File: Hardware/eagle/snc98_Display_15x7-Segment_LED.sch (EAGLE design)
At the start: 67 parts

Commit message: PCB_Display_make
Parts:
- removed C10, C11, C12: 15n, rcl:C-EUC1206K
- removed D1, D10, D11, D12, D13, D29, D3, D4, D5: SD103CW, BaseApp:DIODESMA-WIDE
- removed D6, D7, D8, D9: SD103C, BaseApp:DIODE280MIL-TH
- removed H1, H10, H2, H3, H4, H5, H6, H7, H8, H9: MOUNT-PAD-ROUND2.8, holes:MOUNT-PAD-ROUND2.8
- removed JP1: (no value), SparkFun-Connectors:M09LOCK-LONGPADS
- removed R1, R2, R3: 6k8, rcl:R-EU_R1206
- removed R23, R25, R27: 27k, rcl:R-EU_0204/5
- removed R24, R26, R28: 6k8, rcl:R-EU_0204/5
- removed R4: 27k, rcl:R-EU_R1206
- removed S1, S10, S11, S12, S2, S3, S4, S5, S6, S7, S8, S9: B3F-4150, SmartPrj:TACTILE_SWITCHTACTILE_SWITCH_PTH-12MM
- added BH4, BH5: HOLDER_AAA_LEFT1, SparkFun-Electromechanical:HOLDER_AAA_LEFT1
- added BH6: HOLDER_AAA_RIGHT, SparkFun-Electromechanical:HOLDER_AAA_RIGHT
- added JP10, JP11, JP12, JP7, JP8, JP9: (no value), adafruit:PINHD-1X1
- added LOGO3: OSHW_LOGO_6MILX0100-NT, ohw-logo:OSHW_LOGO_6MILX0100-NT
- added M10, M11, M4, M5, M6, M7, M8, M9: IRLML6402, IRLML6402:IRLML6402
- added R10, R11, R12, R13, R14, R15, R16, R17, R18, R19, R7, R8, R9: 22, rcl:R-EU_R1210
- added R29, R30, R54, R55, R56, R57, R58, R59: 3k3, rcl:R-EU_0204/5
- added R36, R37, R38, R39, R40, R41, R42, R43: 3k3, rcl:R-EU_R1206
- added X1, X3: MICROMATCH-12, Con-amp-micromatch:MICROMATCH-12
- D14, D15, D2: value SD103CW -> SC40-11_UNISC40-11_UNI; device BaseApp:DIODESMA-WIDE -> display-hp:SC40-11_UNISC40-11_UNI
- D16, D17, D18, D19, D20, D21: value BAT54A -> SC40-11_UNISC40-11_UNI; device diode:BAT54A -> display-hp:SC40-11_UNISC40-11_UNI
- D22, D23, D24, D25, D26, D27: value SD103C -> SC40-11_UNISC40-11_UNI; device BaseApp:DIODE280MIL-TH -> display-hp:SC40-11_UNISC40-11_UNI
- R5, R6: value 27k -> 22; device rcl:R-EU_R1206 -> rcl:R-EU_R1210
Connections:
- removed net A1: C10.1, JP1.6, R1.2, R23.1, R24.2, R4.1
- removed net A2: C11.1, JP1.7, R2.2, R25.1, R26.2, R5.1
- removed net A3: C12.1, JP1.8, R27.1, R28.2, R3.2, R6.1
- removed net AREF: JP1.9, R23.2, R25.2, R27.2, R4.2, R5.2, R6.2
- removed net A_1: D1.A, D12.A, D13.A, D16.AA, D17.AA, D23.A, D24.A, D27.A, D29.A, R1.1, R24.1
- removed net A_2: D11.A, D14.A, D18.AA, D19.AA, D2.A, D22.A, D25.A, D26.A, D5.A, R2.1, R26.1
- removed net A_3: D10.A, D15.A, D20.AA, D21.AA, D3.A, D4.A, D6.A, D7.A, D8.A, D9.A, R28.1, R3.1
- removed net C1: JP1.2, S1.1, S1.2, S5.1, S5.2, S9.1, S9.2
- removed net C2: JP1.3, S10.1, S10.2, S2.1, S2.2, S6.1, S6.2
- removed net C3: JP1.4, S11.1, S11.2, S3.1, S3.2, S7.1, S7.2
- removed net C4: JP1.5, S12.1, S12.2, S4.1, S4.2, S8.1, S8.2
- removed net GND: C10.2, C11.2, C12.2, JP1.1, S1.5, S10.5, S11.5, S12.5, S2.5, S3.5, S4.5, S5.5, S6.5, S7.5, S8.5, S9.5
- removed net N$16: D15.C, D20.K1, D6.C, S9.3, S9.4
- removed net N$18: D10.C, D20.K2, D7.C, S10.3, S10.4
- removed net N$19: D12.C, D16.K2, D27.C, S2.3, S2.4
- removed net N$2: D1.C, D17.K2, D23.C, S4.3, S4.4
- removed net N$21: D21.K1, D4.C, D8.C, S11.3, S11.4
- removed net N$22: D21.K2, D3.C, D9.C, S12.3, S12.4
- removed net N$24: D14.C, D18.K1, S5.3, S5.4
- removed net N$25: D11.C, D18.K2, D26.C, S6.3, S6.4
- removed net N$28: D19.K1, D25.C, D5.C, S7.3, S7.4
- removed net N$30: D19.K2, D2.C, D22.C, S8.3, S8.4
- removed net N$32: D17.K1, D24.C, D29.C, S3.3, S3.4
- removed net N$6: D13.C, D16.K1, S1.3, S1.4
- new net CA_LED: M10.S, M11.S, M4.S, M5.S, M6.S, M7.S, M8.S, M9.S, R29.1, R30.1, R36.1, R37.1, R38.1, R39.1, R40.1, R41.1, R42.1, R43.1, R54.1, R55.1, R56.1, R57.1, R58.1, R59.1, X3-8.S
- new net D0_A: R5.2, X3-1.S
- new net D10_A: R15.2, X1-8.S
- new net D11_A: R16.2, X1-9.S
- new net D12_A: R17.2, X1-10.S
- new net D13_A: R18.2, X1-11.S
- new net D14_A: R19.2, X1-12.S
- new net D1_A: R6.2, X3-2.S
- new net D2_A: R7.2, X3-3.S
- new net D3_A: R8.2, X3-4.S
- new net D4_A: R9.2, X3-5.S
- new net D5_A: R10.2, X3-6.S
- new net D6_A: R11.2, X3-7.S
- new net D7_A: R12.2, X1-5.S
- new net D8_A: R13.2, X1-6.S
- new net D9_A: R14.2, X1-7.S
- new net DIG_0: D2.CC1, D2.CC2, D2.CC3, D2.CC4, R5.1
- new net DIG_1: D14.CC1, D14.CC2, D14.CC3, D14.CC4, R6.1
- new net DIG_10: D23.CC1, D23.CC2, D23.CC3, D23.CC4, R15.1
- new net DIG_11: D24.CC1, D24.CC2, D24.CC3, D24.CC4, R16.1
- new net DIG_12: D25.CC1, D25.CC2, D25.CC3, D25.CC4, R17.1
- new net DIG_13: D26.CC1, D26.CC2, D26.CC3, D26.CC4, R18.1
- new net DIG_14: D27.CC1, D27.CC2, D27.CC3, D27.CC4, R19.1
- new net DIG_2: D15.CC1, D15.CC2, D15.CC3, D15.CC4, R7.1
- new net DIG_3: D16.CC1, D16.CC2, D16.CC3, D16.CC4, R8.1
- new net DIG_4: D17.CC1, D17.CC2, D17.CC3, D17.CC4, R9.1
- new net DIG_5: D18.CC1, D18.CC2, D18.CC3, D18.CC4, R10.1
- new net DIG_6: D19.CC1, D19.CC2, D19.CC3, D19.CC4, R11.1
- new net DIG_7: D20.CC1, D20.CC2, D20.CC3, D20.CC4, R12.1
- new net DIG_8: D21.CC1, D21.CC2, D21.CC3, D21.CC4, R13.1
- new net DIG_9: D22.CC1, D22.CC2, D22.CC3, D22.CC4, R14.1
- new net IO-A: M4.G, R29.2, R36.2, X1-4.S
- new net IO-B: M5.G, R30.2, R37.2, X1-3.S
- new net IO-C: M6.G, R42.2, R54.2, X1-2.S
- new net IO-D: M7.G, R38.2, R55.2, X1-1.S
- new net IO-DP: M11.G, R41.2, R59.2, X3-9.S
- new net IO-E: M8.G, R43.2, R56.2, X3-12.S
- new net IO-F: M9.G, R39.2, R57.2, X3-11.S
- new net IO-G: M10.G, R40.2, R58.2, X3-10.S
- new net NC1: BH4.+
- new net NC2: BH5.+
- new net NC3: BH6.-
- new net SEG_A: D14.A, D15.A, D16.A, D17.A, D18.A, D19.A, D2.A, D20.A, D21.A, D22.A, D23.A, D24.A, D25.A, D26.A, D27.A, M4.D
- new net SEG_B: D14.B, D15.B, D16.B, D17.B, D18.B, D19.B, D2.B, D20.B, D21.B, D22.B, D23.B, D24.B, D25.B, D26.B, D27.B, M5.D
- new net SEG_C: D14.C, D15.C, D16.C, D17.C, D18.C, D19.C, D2.C, D20.C, D21.C, D22.C, D23.C, D24.C, D25.C, D26.C, D27.C, JP11.1, JP8.1
- new net SEG_C_SOURCE: JP10.1, M6.D
- new net SEG_D: D14.D, D15.D, D16.D, D17.D, D18.D, D19.D, D2.D, D20.D, D21.D, D22.D, D23.D, D24.D, D25.D, D26.D, D27.D, M7.D
- new net SEG_DP: D14.DP, D14.DP1, D15.DP, D15.DP1, D16.DP, D16.DP1, D17.DP, D17.DP1, D18.DP, D18.DP1, D19.DP, D19.DP1, D2.DP, D2.DP1, D20.DP, D20.DP1, D21.DP, D21.DP1, D22.DP, D22.DP1, D23.DP, D23.DP1, D24.DP, D24.DP1, D25.DP, D25.DP1, D26.DP, D26.DP1, D27.DP, D27.DP1, JP12.1, JP9.1
- new net SEG_DP_SOURCE: JP7.1, M11.D
- new net SEG_E: D14.E, D15.E, D16.E, D17.E, D18.E, D19.E, D2.E, D20.E, D21.E, D22.E, D23.E, D24.E, D25.E, D26.E, D27.E, M8.D
- new net SEG_F: D14.F, D15.F, D16.F, D17.F, D18.F, D19.F, D2.F, D20.F, D21.F, D22.F, D23.F, D24.F, D25.F, D26.F, D27.F, M9.D
- new net SEG_G: D14.G, D14.G1, D15.G, D15.G1, D16.G, D16.G1, D17.G, D17.G1, D18.G, D18.G1, D19.G, D19.G1, D2.G, D2.G1, D20.G, D20.G1, D21.G, D21.G1, D22.G, D22.G1, D23.G, D23.G1, D24.G, D24.G1, D25.G, D25.G1, D26.G, D26.G1, D27.G, D27.G1, M10.D
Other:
- note added: "0.8"
- note added: "Calculator 15-Digit with 1284P"
- note added: "Calculator 15-Digit with ATmega1284P by Jens Grabner is licensed under"
- note removed: "0.3"
- note removed: "snc98 3x4 Switch-block"
- note removed: "snc98 3x4 Switch-block Rev. 0.3 by Jens Grabner is licensed under"

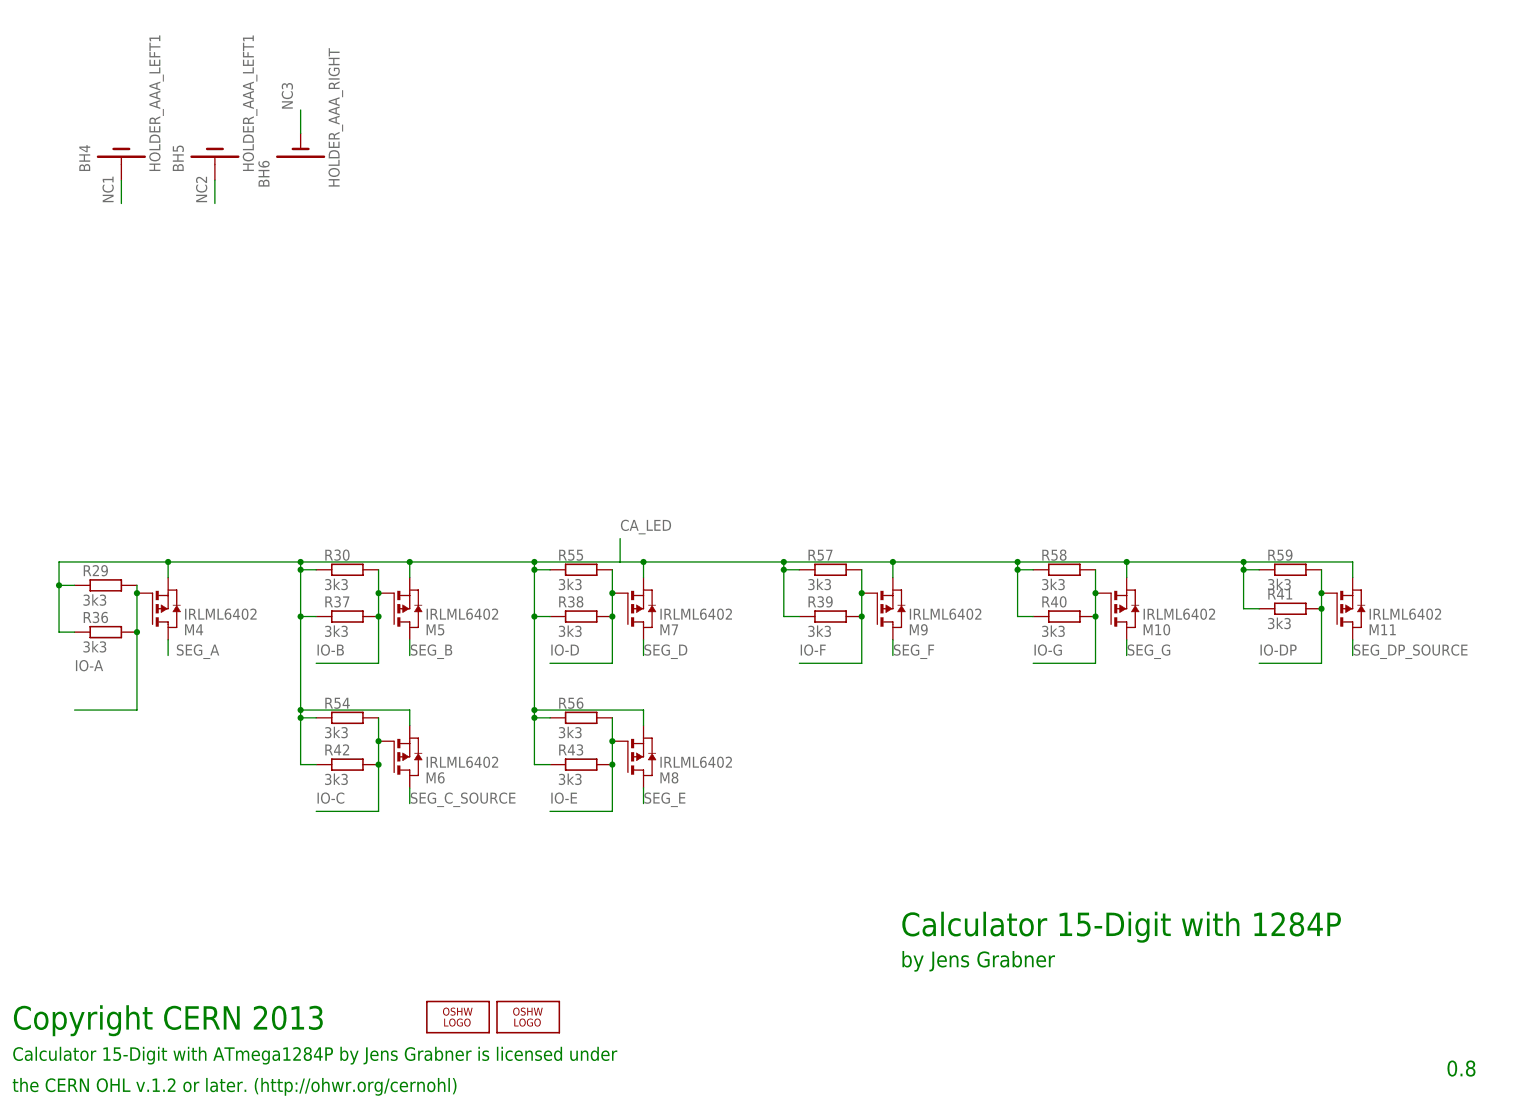
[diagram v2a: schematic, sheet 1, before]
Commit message: snc98_Display_15x7-Segment_LED_v2
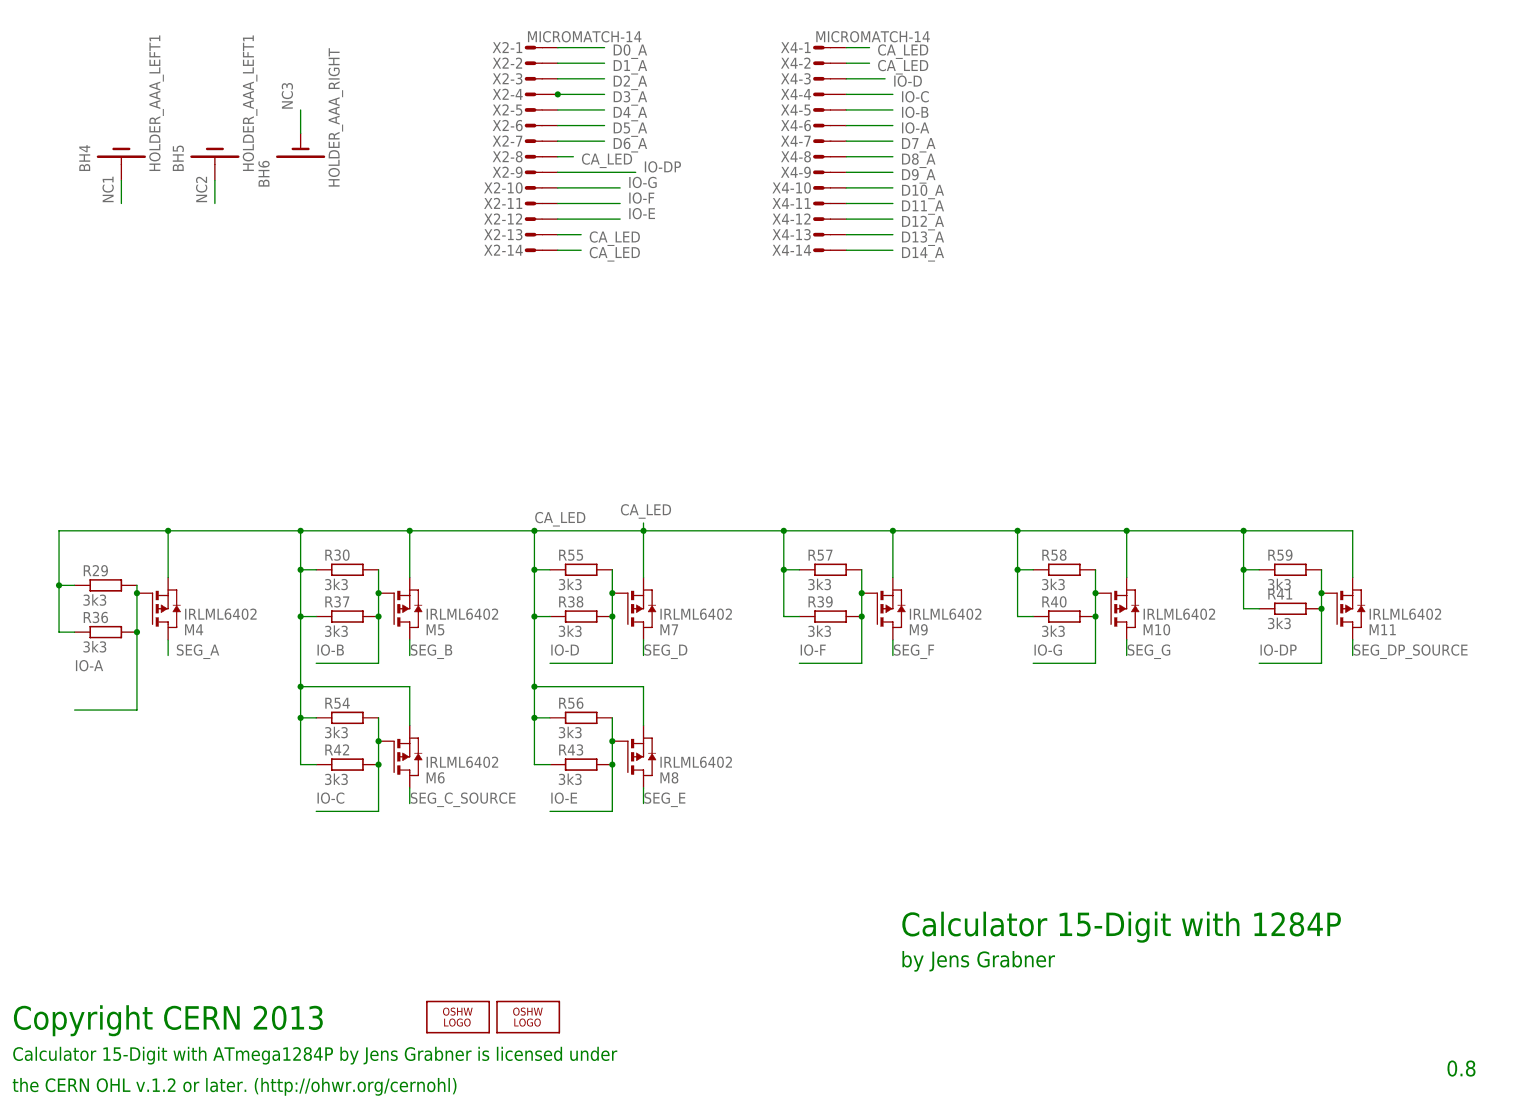
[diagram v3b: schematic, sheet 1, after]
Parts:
- added JP1, JP2: (no value), adafruit:PINHD-1X1
- added X2, X4: MICROMATCH-14, Con-amp-micromatch:MICROMATCH-14
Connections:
- net CA_LED: now also JP1.1, JP2.1, X2-13.S, X2-14.S, X2-8.S, X4-1.S, X4-2.S
- net D0_A: now also X2-1.S
- net D10_A: now also X4-10.S
- net D11_A: now also X4-11.S
- net D12_A: now also X4-12.S
- net D13_A: now also X4-13.S
- net D14_A: now also X4-14.S
- net D1_A: now also X2-2.S
- net D2_A: now also X2-3.S
- net D3_A: now also X2-4.S
- net D4_A: now also X2-5.S
- net D5_A: now also X2-6.S
- net D6_A: now also X2-7.S
- net D7_A: now also X4-7.S
- net D8_A: now also X4-8.S
- net D9_A: now also X4-9.S
- net IO-A: now also X4-6.S
- net IO-B: now also X4-5.S
- net IO-C: now also X4-4.S
- net IO-D: now also X4-3.S
- net IO-DP: now also X2-9.S
- net IO-E: now also X2-12.S
- net IO-F: now also X2-11.S
- net IO-G: now also X2-10.S
